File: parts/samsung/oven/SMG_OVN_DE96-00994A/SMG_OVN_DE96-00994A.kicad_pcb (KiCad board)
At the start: 2 copper layers, 78.5 x 137.9 mm, 28 parts

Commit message: Minor design modifications
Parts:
- removed the REF** at (47.5, 5.00)
- added G***: LOGO, OpenSpare_footprints:OpenSpare-Logo_Text_20x20mm_SilkScreen, F.Cu at (27.5, 9.53)
- added G***: LOGO, OpenSpare_footprints:OpenSpare-QRCode_Github_10x10mm_SilkScreen, B.Cu at (5.25, 52.0)
- added J1: Conn_01x04_Socket, Connector_JST:JST_XH_S4B-XH-A_1x04_P2.50mm_Horizontal, F.Cu at (23.7, 47.6)
- RS1: renamed from S1; value SRRM1C7800 -> 4P3T Rotary Switch
- moved R9 120.3 mm to (21.6, 18.2), turned to 0 degrees
- moved R10 119.9 mm to (27.6, 16.5), turned to 0 degrees
- moved R8 118.1 mm to (16.0, 22.9)
- moved R15 113.4 mm to (22.2, 13.8), turned to -90 degrees
- moved R7 112.2 mm to (16.0, 28.4)
- moved R16 110.6 mm to (12.8, 28.8), turned to -90 degrees
- moved R5 107.6 mm to (21.6, 39.8), turned to 0 degrees
- moved R11 107.4 mm to (33.2, 18.2), turned to 0 degrees
- moved R6 105.8 mm to (16.0, 34.6), turned to -90 degrees
- moved R1 102.3 mm to (40.0, 28.8), turned to 0 degrees
- moved R12 101.9 mm to (38.8, 22.8), turned to -90 degrees
- moved R4 101.6 mm to (27.3, 41.0), turned to 0 degrees
- moved R14 101.1 mm to (40.0, 13.8), turned to -90 degrees
- moved R2 98.5 mm to (38.8, 34.7)
- moved R3 97.9 mm to (33.3, 39.8), turned to 0 degrees
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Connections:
- net Net-(D1-K) renamed /LED_K
- net Net-(R13-Pad1) renamed /OUT
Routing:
- net /LED_K: track 0.00 -> 156.8 mm
- net VDD: track 0.00 -> 96.1 mm
- net /OUT: track 0.00 -> 21.7 mm
- net Net-(R8-Pad2): track 0.00 -> 9.07 mm
- net Net-(R5-Pad1): track 0.00 -> 9.04 mm
- net Net-(R2-Pad1): track 0.00 -> 8.84 mm
- net Net-(R11-Pad2): track 0.00 -> 8.54 mm
- net Net-(R1-Pad1): track 0.00 -> 7.30 mm
- net Net-(R3-Pad1): track 0.00 -> 7.11 mm
- net Net-(R4-Pad1): track 0.00 -> 7.01 mm
- net Net-(D1-A): track 0.00 -> 7.01 mm
- net Net-(R10-Pad1): track 0.00 -> 6.98 mm
- net Net-(R10-Pad2): track 0.00 -> 6.79 mm
- net Net-(R6-Pad1): track 0.00 -> 6.72 mm
- net Net-(R7-Pad2): track 0.00 -> 6.33 mm
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- added copper zone on B.Cu, net /OUT
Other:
- board size 78.5 x 137.9 mm -> 55 x 57.2 mm
- board text added: "Ref: SMG_OVN_DE96-00994A Date: 09/2025 Rev: 01 Status: Not tested"

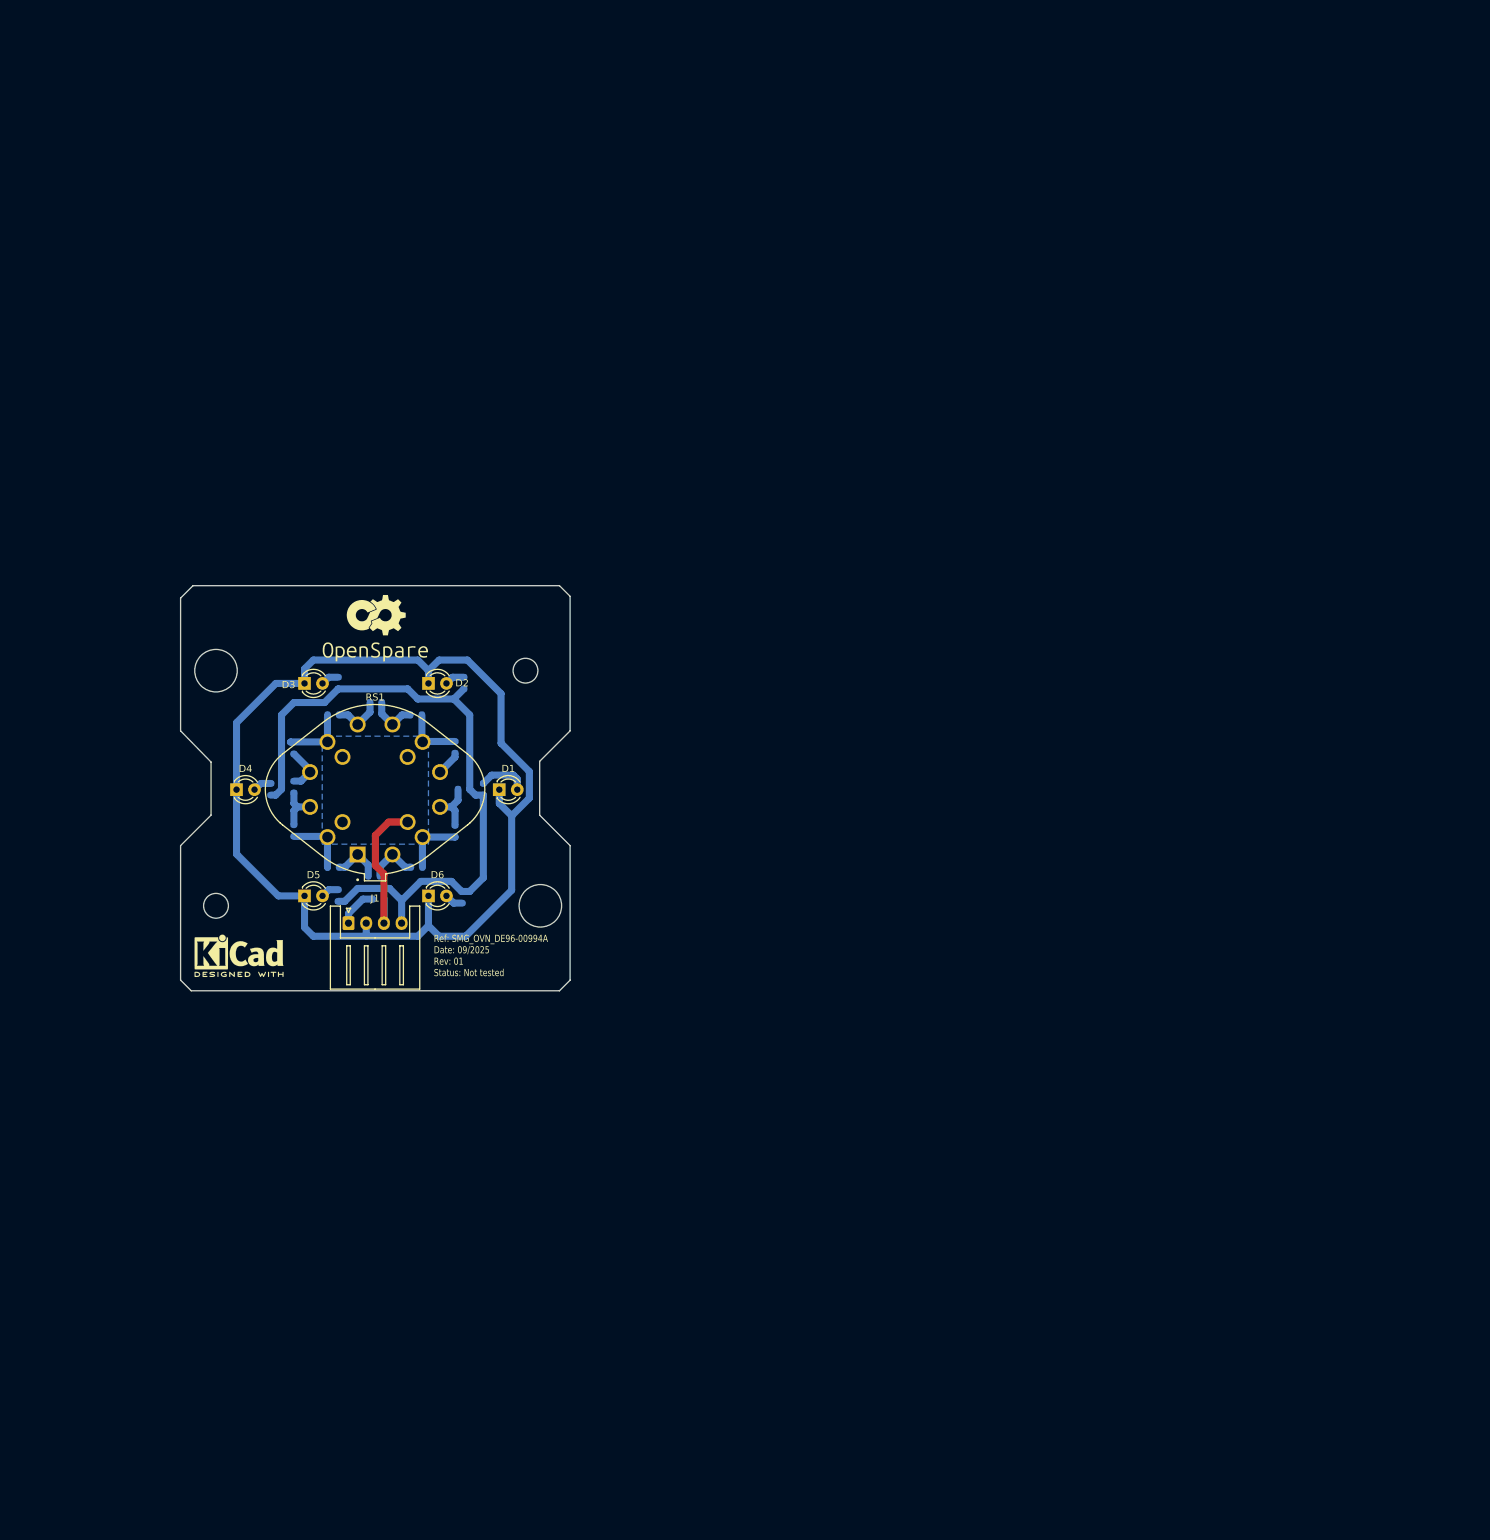
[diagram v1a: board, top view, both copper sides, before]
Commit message: Update SMG_OVN_DE96-00994A design (rev 1)
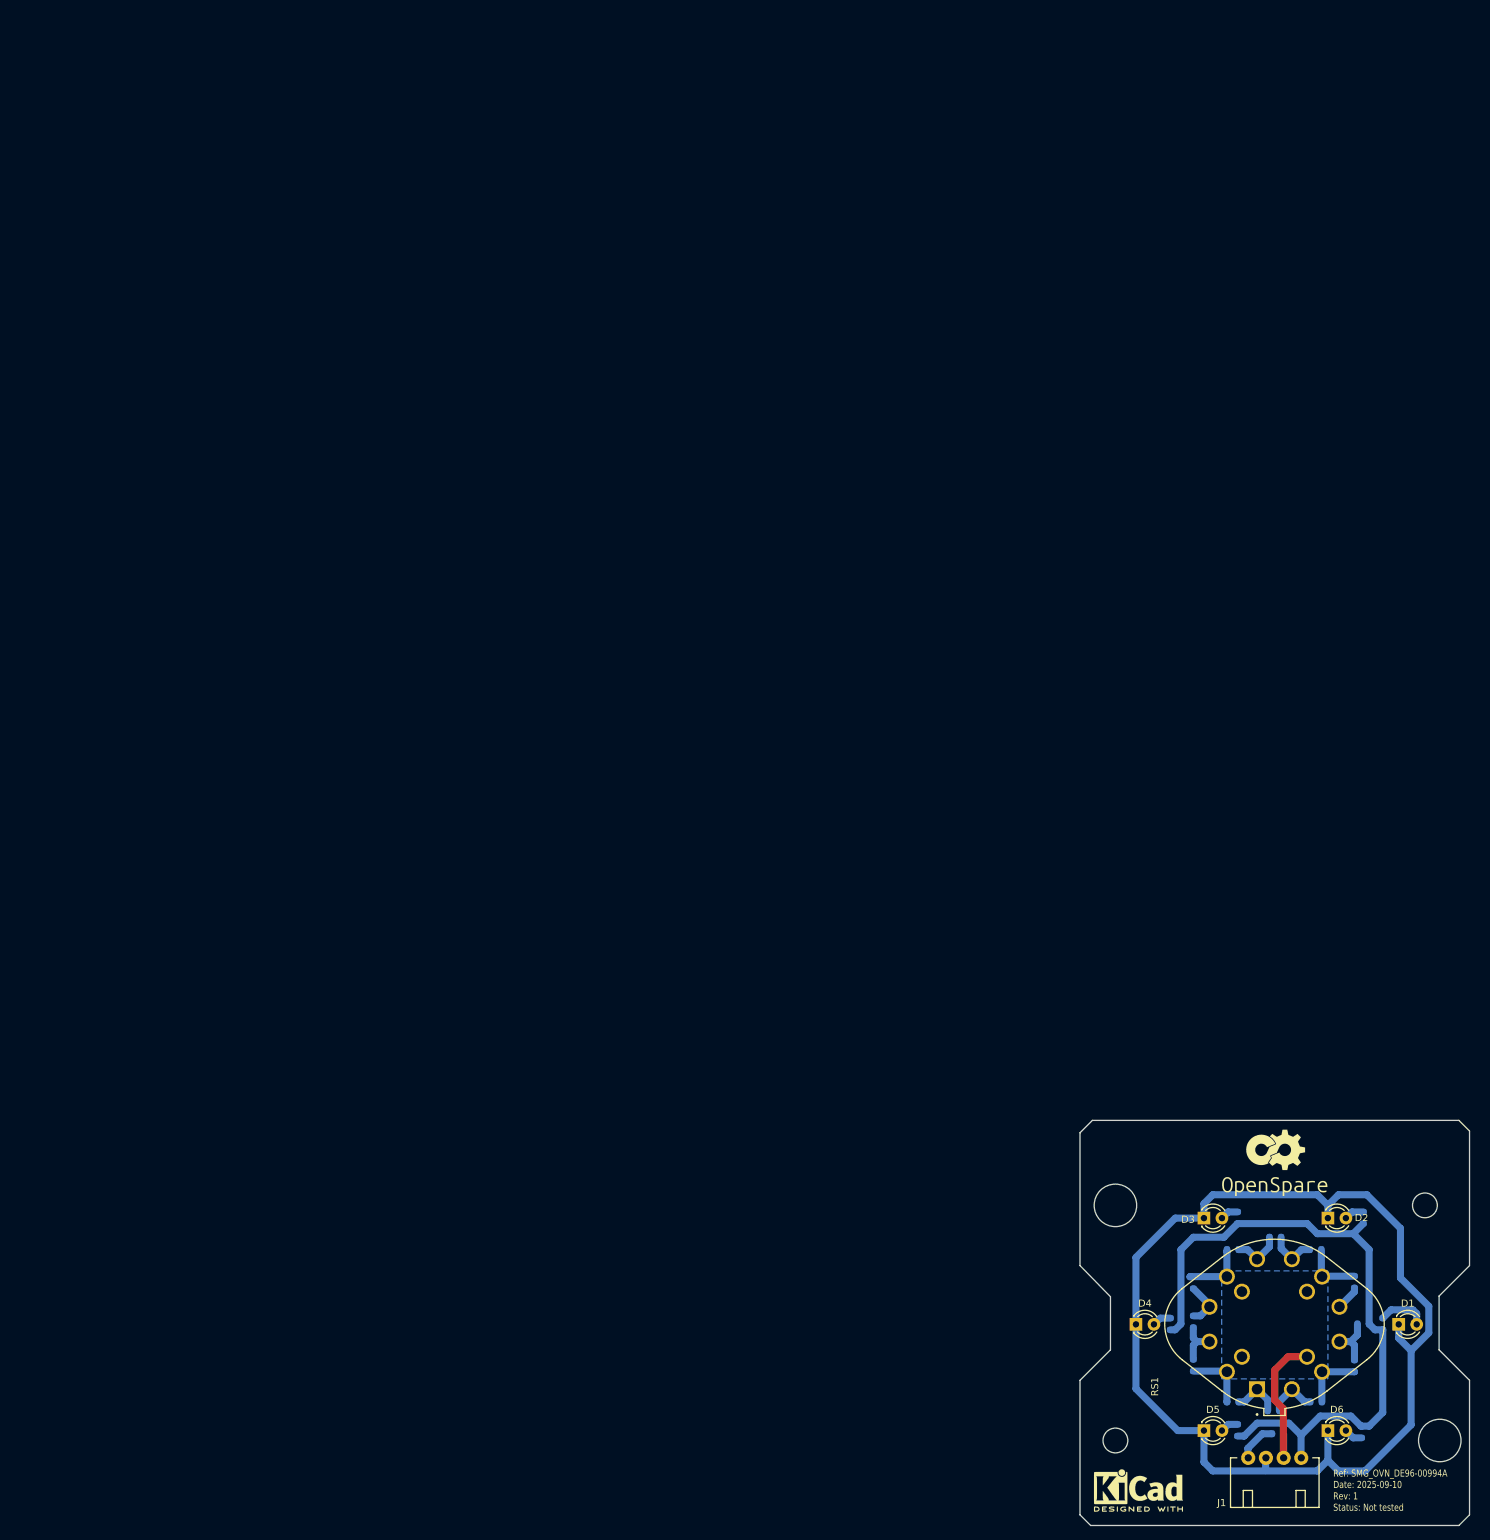
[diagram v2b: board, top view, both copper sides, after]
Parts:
- G***: footprint OpenSpare_footprints:OpenSpare-Logo_Text_20x20mm_SilkScreen -> OpenSpare_footprints:OpenSpare-Logo_Text_15x9mm_SilkScreen
- J1: footprint Connector_JST:JST_XH_S4B-XH-A_1x04_P2.50mm_Horizontal -> OpenSpare_footprints:KON_C2502RD10403T0101PB
- R14, R15, R16, R17, R18, R19: value 10k -> ~
- RS1: footprint OpenSpare_footprints:SW_SRRM1C7800 -> OpenSpare_footprints:SW_RS240403A0X-HA1-000
- moved J1 147.8 mm to (150.8, 123.2)
- moved R13 147.7 mm to (154.9, 119.8)
- moved D1 147.7 mm to (172.0, 104.3)
- moved D2 147.7 mm to (162.0, 89.3)
- moved D3 147.7 mm to (144.5, 89.3)
- moved D4 147.7 mm to (134.9, 104.3)
- moved D5 147.7 mm to (144.5, 119.3)
- moved D6 147.7 mm to (162.0, 119.3)
- moved G*** 147.7 mm to (154.5, 85.0)
- moved G*** 147.7 mm to (132.2, 127.5)
- moved R1 147.7 mm to (167.0, 104.2)
- moved R10 147.7 mm to (154.6, 92.0)
- moved R11 147.7 mm to (160.2, 93.8)
- moved R12 147.7 mm to (165.8, 98.3)
- moved R14 147.7 mm to (167.0, 89.2)
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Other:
- outline, holes or cut-outs redrawn
- board text added: "Ref: ${TITLE} Date: ${ISSUE_DATE} Rev: ${REVISION} Status: Not tested"
- board text removed: "Ref: SMG_OVN_DE96-00994A Date: 09/2025 Rev: 01 Status: Not tested"

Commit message: Generate output for JLCPCB format
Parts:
- R11, R12: value 4,7k -> 4.7k
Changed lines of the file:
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@@
 			)
 		)
+		(property "LCSC Part #" "C9900221323"
+			(at 0 0 0)
+			(unlocked yes)
+			(layer "F.Fab")
+			(hide yes)
+			(effects
+				(font
+					(size 1 1)
+					(thickness 0.15)
+				)
+			)
+		)
 		(sheetname "/")
 		(sheetfile "SMG_OVN_DE96-00994A.kicad_sch")
@@
 			)
 		)
+		(property "LCSC Part #" "C9900221322"
+			(at 0 0 90)
+			(unlocked yes)
+			(layer "F.Fab")
+			(hide yes)
+			(effects
+				(font
+					(size 1 1)
+					(thickness 0.15)
+				)
+			)
+		)
 		(sheetname "/")
 		(sheetfile "SMG_OVN_DE96-00994A.kicad_sch")
@@
 			)
 		)
+		(property "LCSC Part #" "C1512170"
+			(at 0 0 0)
+			(unlocked yes)
+			(layer "B.Fab")
+			(hide yes)
+			(effects
+				(font
+					(size 1 1)
+					(thickness 0.15)
+				)
+				(justify mirror)
+			)
+		)
 		(property ki_fp_filters "R_*")
 		(sheetname "/")
@@
 			)
 		)
+		(property "LCSC Part #" "C1512170"
+			(at 0 0 90)
+			(unlocked yes)
+			(layer "B.Fab")
+			(hide yes)
+			(effects
+				(font
+					(size 1 1)
+					(thickness 0.15)
+				)
+				(justify mirror)
+			)
+		)
 		(property ki_fp_filters "R_*")
 		(sheetname "/")
@@
 			)
 		)
-		(property "Description" "Thick Film Resistors - SMD General Purpose Chip Resistor 0603, 10kOhms, 5%, 1/10W"
+		(property "Description" "Thick Film Resistors - SMD General Purpose Chip Resistor 0603, 10kOhms, 1%, 1/10W"
 			(at 0 0 0)
 			(layer "B.Fab")
@@
 			)
 		)
-		(property "Supplier1_Part_Number" "603-RC0603JR-0710KL"
+		(property "Supplier1_Part_Number" " 603-RC0603FR-1010KL"
 			(at 0 0 180)
 			(unlocked yes)
@@
 			)
 		)
-		(property "Manufacturer1_Part_Number" "RC0603JR-0710KL"
+		(property "Manufacturer1_Part_Number" "RC0603FR-1010KL"
 			(at 0 0 180)
 			(unlocked yes)
@@
 			)
 		)
+		(property "LCSC Part #" "C4004838"
+			(at 0 0 180)
+			(unlocked yes)
+			(layer "B.Fab")
+			(hide yes)
+			(effects
+				(font
+					(size 1 1)
+					(thickness 0.15)
+				)
+				(justify mirror)
+			)
+		)
 		(property ki_fp_filters "R_*")
 		(sheetname "/")
@@
 			)
 		)
-		(property "Value" "4,7k"
+		(property "Value" "4.7k"
 			(at 0 -1.43 0)
 			(layer "B.Fab")
@@
 			)
 		)
+		(property "LCSC Part #" "C4269355"
+			(at 0 0 0)
+			(unlocked yes)
+			(layer "B.Fab")
+			(hide yes)
+			(effects
+				(font
+					(size 1 1)
+					(thickness 0.15)
+				)
+				(justify mirror)
+			)
+		)
 		(property ki_fp_filters "R_*")
 		(sheetname "/")
@@
 			)
 		)
+		(property "LCSC Part #" "C1512170"
+			(at 0 0 0)
+			(unlocked yes)
+			(layer "B.Fab")
+			(hide yes)
+			(effects
+				(font
+					(size 1 1)
+					(thickness 0.15)
+				)
+				(justify mirror)
+			)
+		)
 		(property ki_fp_filters "R_*")
 		(sheetname "/")
@@
 			)
 		)
+		(property "LCSC Part #" "C4103683"
+			(at 0 0 90)
+			(unlocked yes)
+			(layer "B.Fab")
+			(hide yes)
+			(effects
+				(font
+					(size 1 1)
+					(thickness 0.15)
+				)
+				(justify mirror)
+			)
+		)
 		(property ki_fp_filters "R_*")
 		(sheetname "/")
@@
 			)
 		)
+		(property "LCSC Part #" "C1512170"
+			(at 0 0 0)
+			(unlocked yes)
+			(layer "B.Fab")
+			(hide yes)
+			(effects
+				(font
+					(size 1 1)
+					(thickness 0.15)
+				)
+				(justify mirror)
+			)
+		)
 		(property ki_fp_filters "R_*")
 		(sheetname "/")
@@
 			)
 		)
+		(property "LCSC Part #" "C4103683"
+			(at 0 0 0)
+			(unlocked yes)
+			(layer "B.Fab")
+			(hide yes)
+			(effects
+				(font
+					(size 1 1)
+					(thickness 0.15)
+				)
+				(justify mirror)
+			)
+		)
 		(property ki_fp_filters "R_*")
 		(sheetname "/")
@@
 			)
 		)
+		(property "LCSC Part #" "C4103683"
+			(at 0 0 90)
+			(unlocked yes)
+			(layer "B.Fab")
+			(hide yes)
+			(effects
+				(font
+					(size 1 1)
+					(thickness 0.15)
+				)
+				(justify mirror)
+			)
+		)
 		(property ki_fp_filters "R_*")
 		(sheetname "/")
@@
 			)
 		)
+		(property "LCSC Part #" "C1512170"
+			(at 0 0 0)
+			(unlocked yes)
+			(layer "B.Fab")
+			(hide yes)
+			(effects
+				(font
+					(size 1 1)
+					(thickness 0.15)
+				)
+				(justify mirror)
+			)
+		)
 		(property ki_fp_filters "R_*")
 		(sheetname "/")
@@
 			)
 		)
+		(property "LCSC Part #" "C4103683"
+			(at 0 0 0)
+			(unlocked yes)
+			(layer "B.Fab")
+			(hide yes)
+			(effects
+				(font
+					(size 1 1)
+					(thickness 0.15)
+				)
+				(justify mirror)
+			)
+		)
 		(property ki_fp_filters "R_*")
 		(sheetname "/")
@@
 			)
 		)
+		(property "LCSC Part #" "C1512170"
+			(at 0 0 270)
+			(unlocked yes)
+			(layer "B.Fab")
+			(hide yes)
+			(effects
+				(font
+					(size 1 1)
+					(thickness 0.15)
+				)
+				(justify mirror)
+			)
+		)
 		(property ki_fp_filters "R_*")
 		(sheetname "/")
@@
 			)
 		)
-		(property "Value" "4,7k"
+		(property "Value" "4.7k"
 			(at 0 -1.43 90)
 			(layer "B.Fab")
@@
 			(at 0 0 270)
 			(unlocked yes)
+			(layer "B.Fab")
+			(hide yes)
+			(effects
+				(font
+					(size 1 1)
+					(thickness 0.15)
+				)
+				(justify mirror)
+			)
+		)
+		(property "LCSC Part #" "C4269355"
+			(at 0 0 270)
+			(unlocked yes)

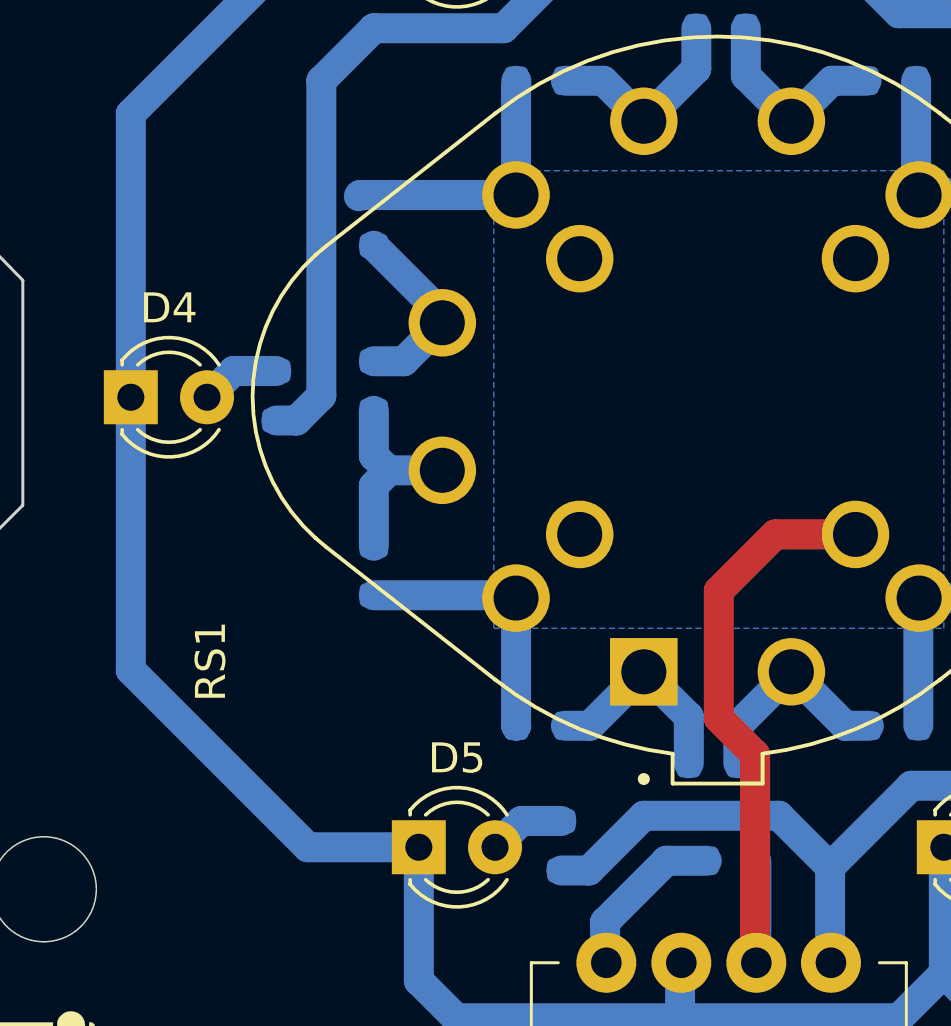
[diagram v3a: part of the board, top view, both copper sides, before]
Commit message: Minor PCB fixes
- Remove excess of copper  near R8
- Fix placement of RS1 label
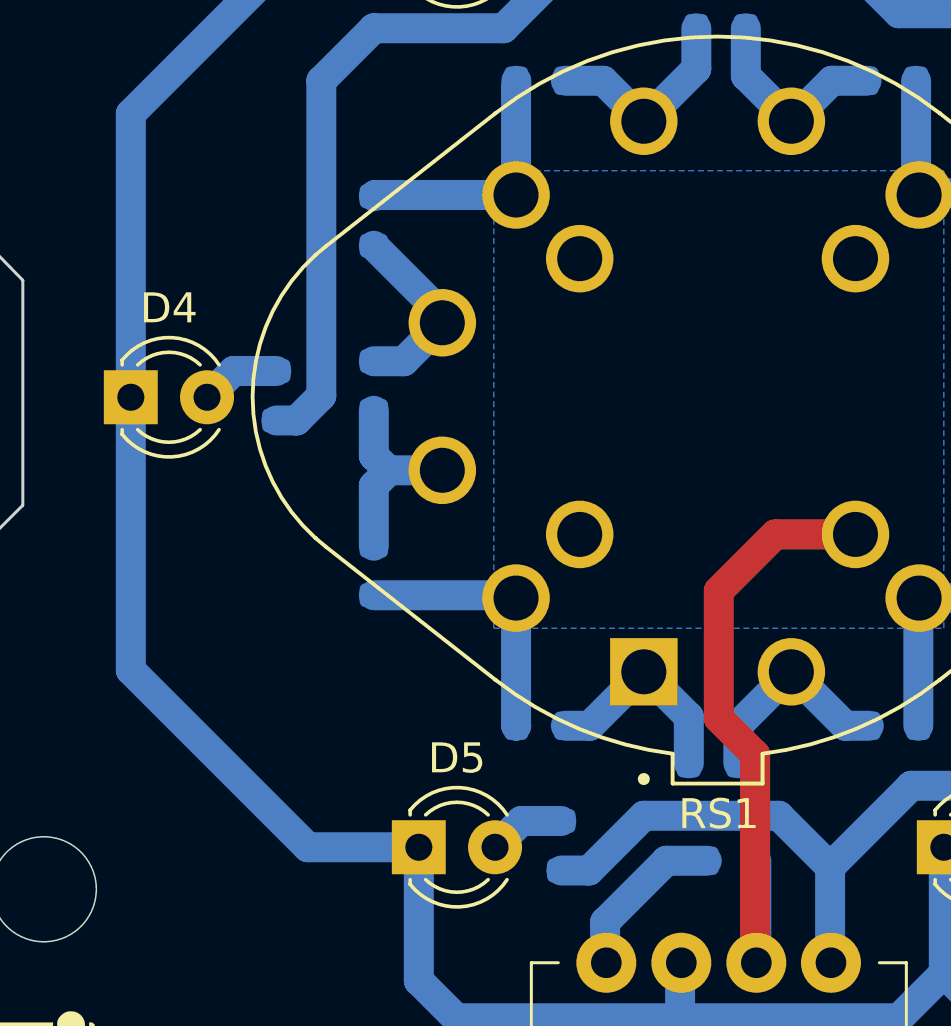
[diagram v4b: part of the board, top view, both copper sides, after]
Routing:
- net Net-(R8-Pad2): track 9.07 -> 8.57 mm
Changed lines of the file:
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@@
 		(at 154.459 104.276 90)
 		(property "Reference" "RS1"
-			(at -8.825 -16.885 90)
+			(at -13.924 0.041 180)
 			(layer "F.SilkS")
 			(effects
@@
 	)
 	(segment
-		(start 147.75 93.75)
-		(end 147.75 94)
+		(start 147.741 97.558)
+		(end 143.042 97.558)
 		(width 1)
-		(locked yes)
 		(layer "B.Cu")
 		(net 9)
 	)
 	(segment
-		(start 142.542 97.558)
-		(end 142.5 97.6)
+		(start 147.75 93.75)
+		(end 147.75 94)
 		(width 1)
 		(locked yes)
@@
 	)
 	(segment
-		(start 147.741 97.558)
-		(end 142.542 97.558)
+		(start 143.042 97.558)
+		(end 143 97.6)
 		(width 1)
-		(locked yes)
 		(layer "B.Cu")
 		(net 9)
